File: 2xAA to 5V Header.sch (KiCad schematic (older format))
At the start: 9 parts, among them SW1 SPDT, U1 LTC3426

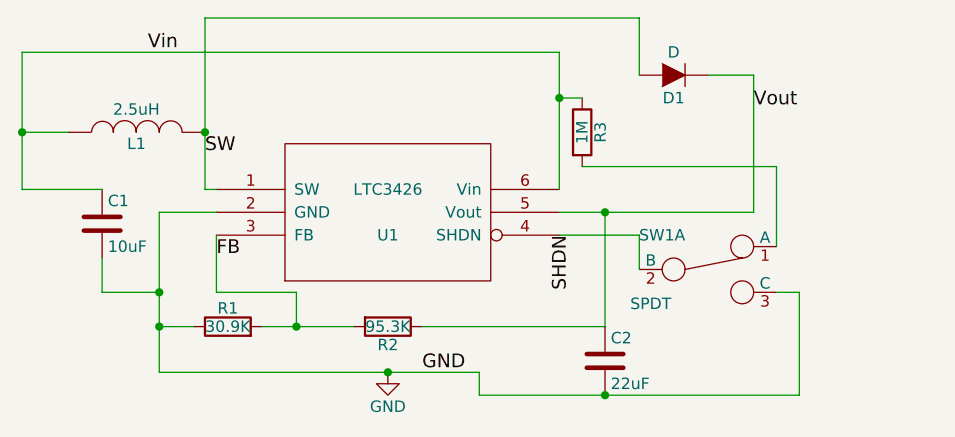
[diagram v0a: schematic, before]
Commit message: Pin header and corners
Added a two pin header for the output to make attaching leads easier and
cleaned up any 90 degree corners in fills.
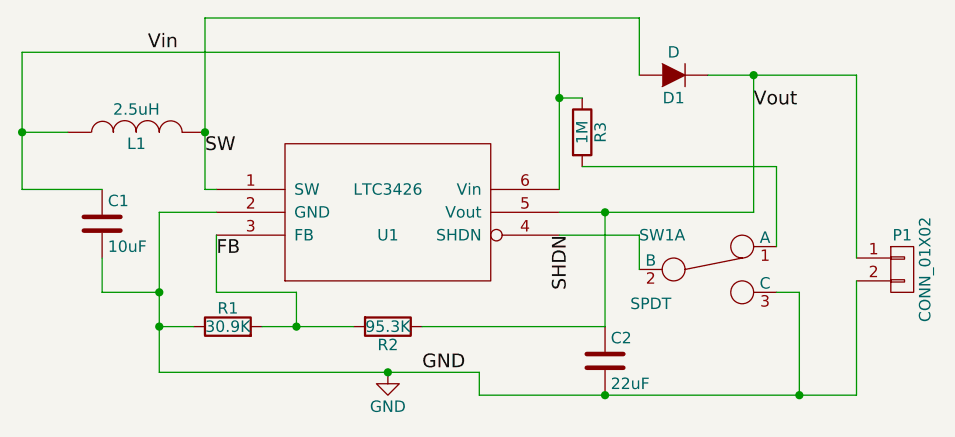
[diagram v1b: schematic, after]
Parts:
- added P1: CONN_01X02, Pin_Headers:Pin_Header_Angled_1x02, symbol CONN_01X02
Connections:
- net GND: now also P1.2 (P2)
- net Vout: now also P1.1 (P1)
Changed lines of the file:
@@
 $EndComp
 Wire Wire Line
-	6000 3800 7400 3800
+	6000 3800 7650 3800
 Wire Wire Line
 	6000 3700 6000 3800
 Connection ~ 5600 3700
 Wire Wire Line
-	7000 2400 7200 2400
+	7000 2400 7650 2400
 Connection ~ 6550 3000
 Wire Wire Line
@@
 	4000 2300 6350 2300
 Wire Wire Line
-	7200 2400 7200 3000
+	7200 3000 7200 2400
 Text Label 7200 2550 0    60   ~ 0
 Vout
@@
 Wire Wire Line
 	7400 3350 7300 3350
+$Comp
+L CONN_01X02 P1
+U 1 1 56FA9DBF
+P 7850 3250
+F 0 "P1" H 7850 3400 50  0000 C CNN
+F 1 "CONN_01X02" V 7950 3250 50  0000 C CNN
+F 2 "Pin_Headers:Pin_Header_Angled_1x02" H 7850 3250 50  0001 C CNN
+F 3 "" H 7850 3250 50  0000 C CNN
+	1    7850 3250
+	1    0    0    -1
+$EndComp
+Wire Wire Line
+	7650 2400 7650 3200
+Connection ~ 7200 2400
+Wire Wire Line
+	7650 3800 7650 3300
+Connection ~ 7400 3800
 $EndSCHEMATC
